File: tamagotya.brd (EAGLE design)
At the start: 27.9 x 31.8 mm, 64 parts, among them U100 ESP32-D2WD, U1000 TP4056, U1500 FS312F-G, U1550 FS8205, U200 UT-0206-P05FOLDED, U2000 MT3608, U2100 M3406, U300 4MB Flash, Y100 40Mhz 3.2X2.5

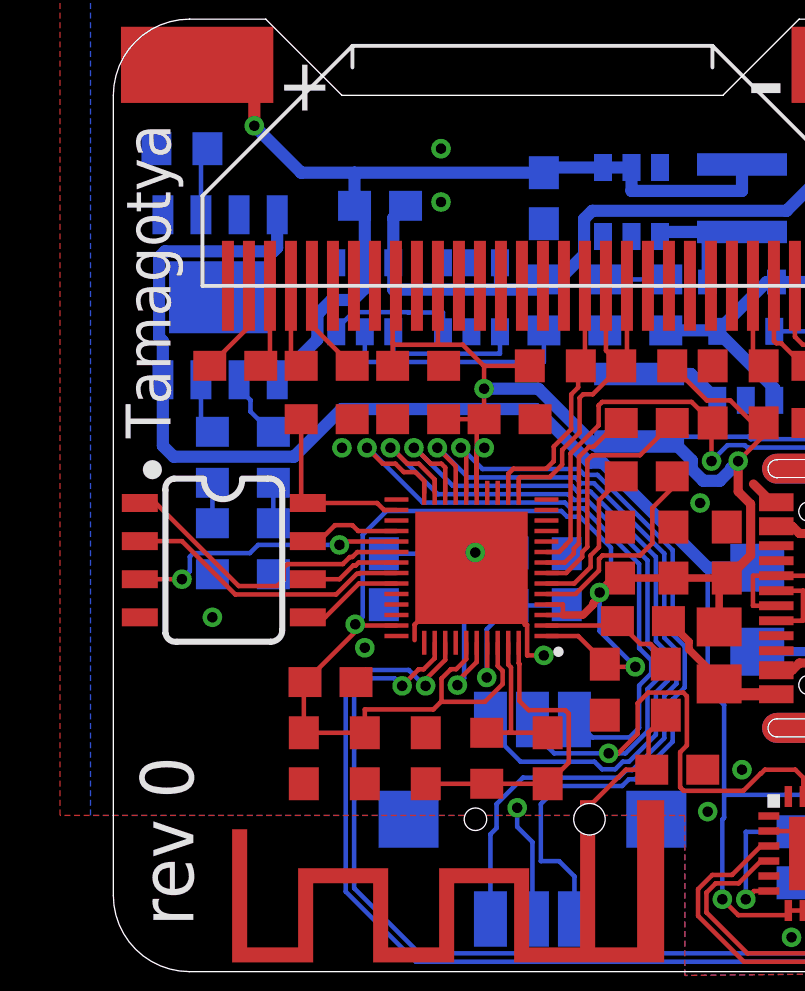
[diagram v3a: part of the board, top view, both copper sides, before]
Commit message: Accellerometer ADXL345 with i2c + 1 interrupt.
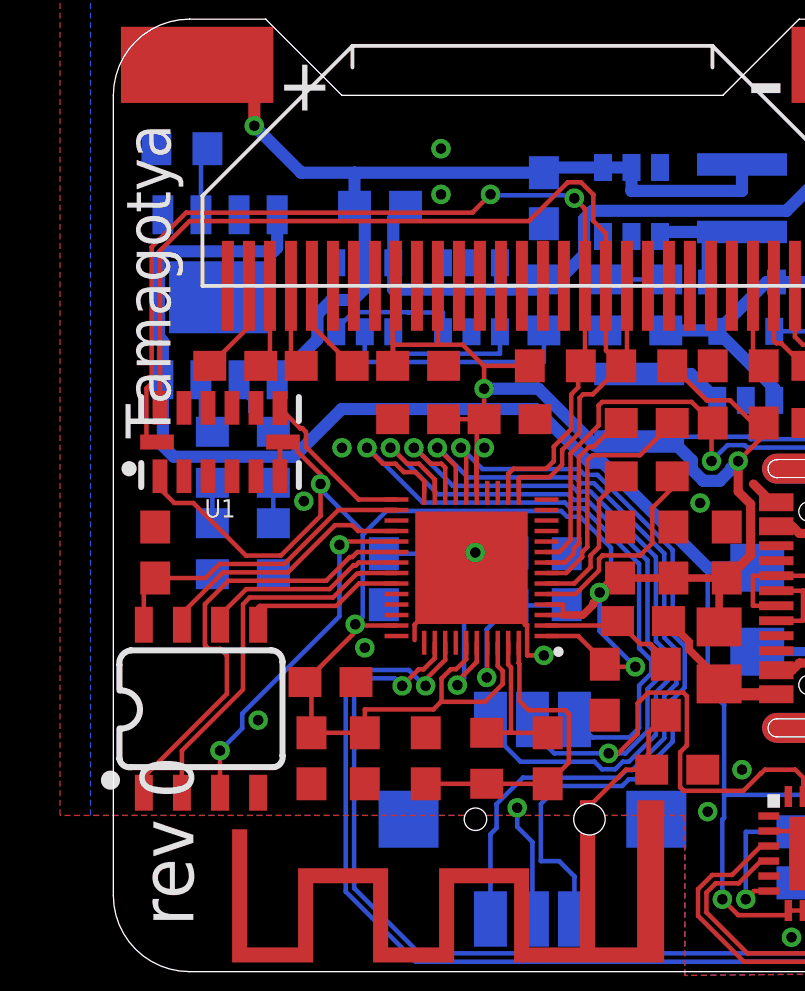
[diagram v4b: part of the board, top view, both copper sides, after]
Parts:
- added U1: ADXL345, SparkFun-Sensors:LGA-14
- moved C300 7.24 mm to (1.40, 14.0), turned to 90 degrees
- moved U300 5.01 mm to (2.92, 8.76), turned to 0 degrees
- moved C111 0.25 mm to (6.60, 7.11)
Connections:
- net 3.3V: now also U1.1, U1.6, U1.7
- net GND: now also U1.12, U1.2, U1.4, U1.5
- net GPIO16: now also U1.8
- net SCL: now also U1.14
- net SDA: now also U1.13
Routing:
- net SCL: track 8.60 -> 33.5 mm, vias 0 -> 2
- net SDA: track 12.1 -> 36.2 mm
- net 3.3V: track 91.9 -> 105.7 mm, vias 6 -> 7
- net SHD/SD2: track 3.26 -> 8.83 mm
- net VDD_SDIO: track 5.94 -> 11.4 mm
- net GPIO16: track 0.00 -> 5.43 mm
- net SCS/CMD: track 10.4 -> 15.1 mm
- net SCK/CLK: track 3.19 -> 6.92 mm
- net SDO/SD0: track 9.59 -> 12.7 mm
- net SWP/SD3: track 9.36 -> 11.9 mm
- net SDI/SD1: track 3.42 -> 5.52 mm
- net GND: vias 14 -> 15
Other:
- board text added: "TODO: Attach charge status circuitry to something ADC sensing battery voltage. DAC output for small speaker ESP32 TX/RX/RST/GPIO-0 breakout I2C breakout?"
- board text removed: "TODO: ADC sensing battery voltage. DAC output for small speaker ESP32 TX/RX/RST/GPIO-0 breakout Accellerometer would be reet grand I2C breakout?"

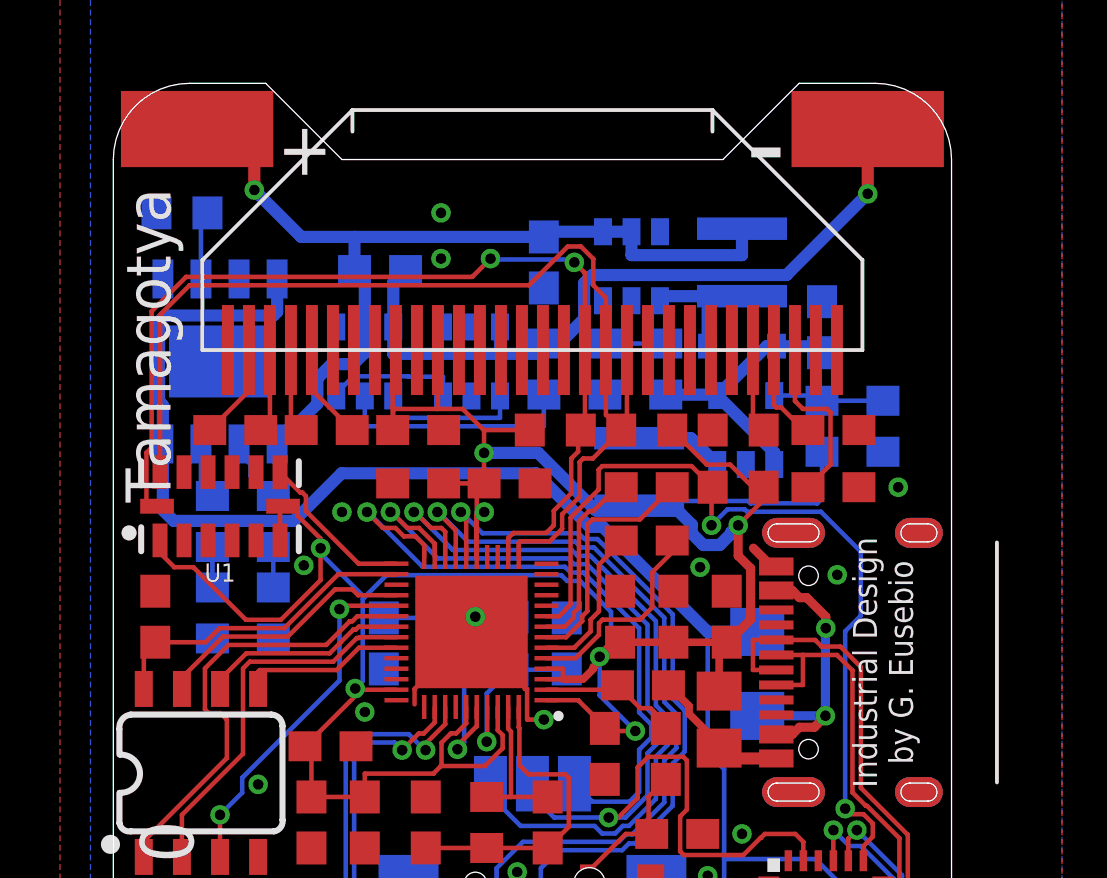
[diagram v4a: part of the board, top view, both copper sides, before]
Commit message: Done: ADC sensing battery voltage.
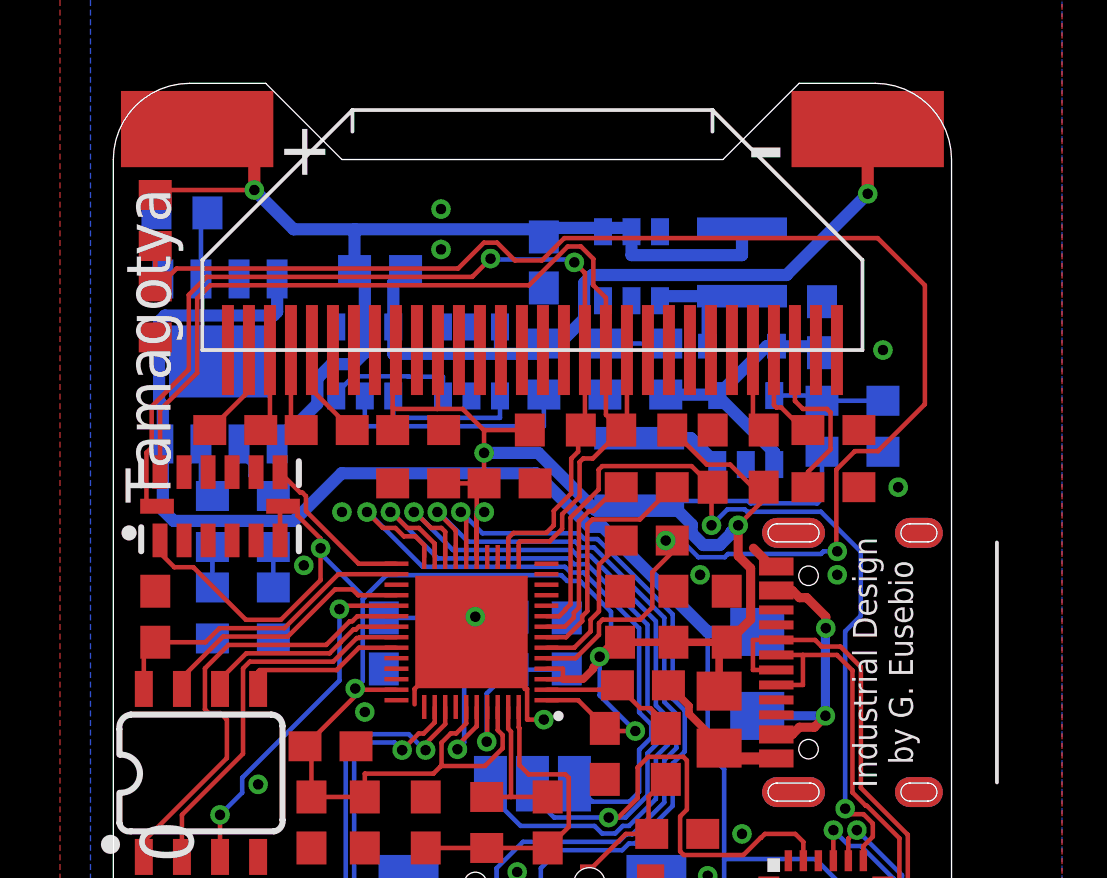
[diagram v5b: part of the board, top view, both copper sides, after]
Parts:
- added R4, R5: 20k, rcl:R0603
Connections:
- net GND: now also R5.1
- net SENSOR_VP: now also R4.1, R5.2
- net V_BATT: now also R4.2
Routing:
- net SENSOR_VP: track 6.96 -> 52.6 mm, vias 0 -> 2
- net V_BATT: track 31.6 -> 35.5 mm
- net VDD_SDIO: track 11.4 -> 10.7 mm
- net GND: vias 15 -> 16
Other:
- board text added: "TODO: DAC output for small speaker ESP32 TX/RX/RST/GPIO-0 breakout I2C breakout?"
- board text removed: "TODO: Attach charge status circuitry to something ADC sensing battery voltage. DAC output for small speaker ESP32 TX/RX/RST/GPIO-0 breakout I2C breakout?"

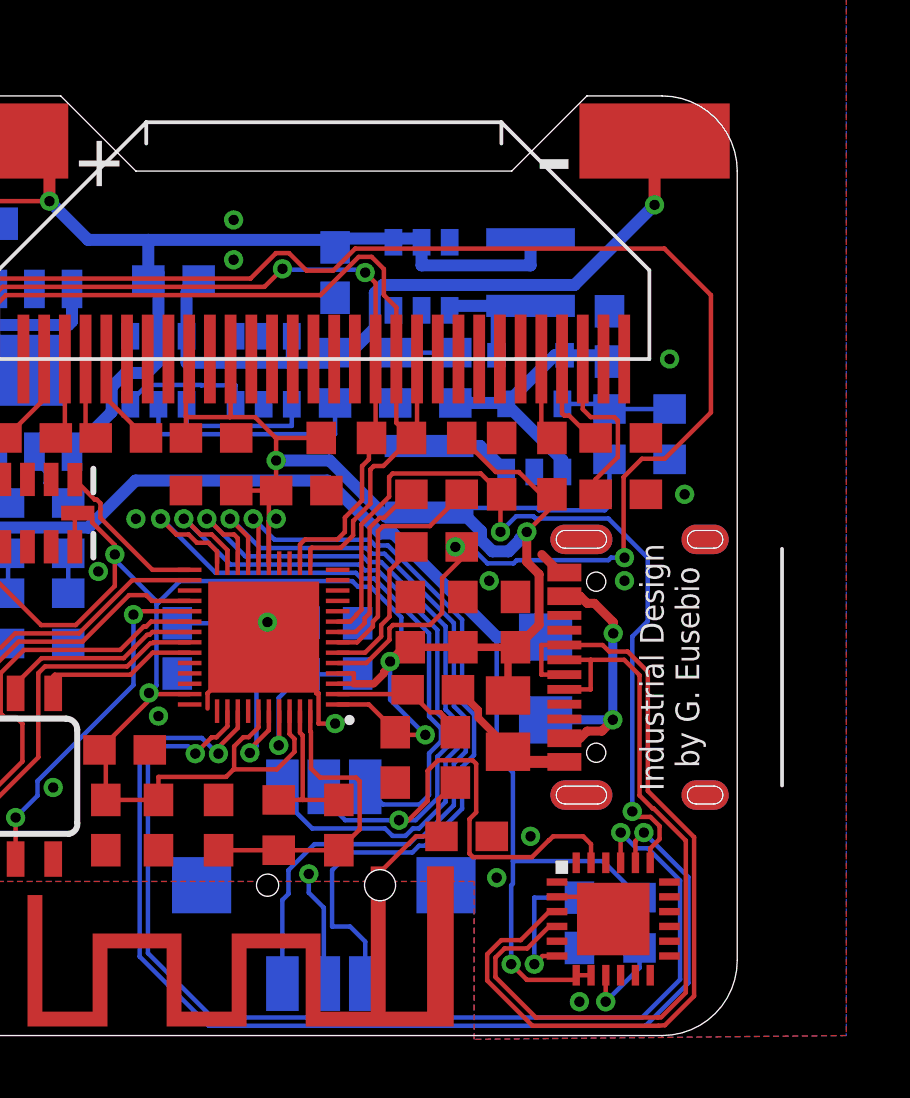
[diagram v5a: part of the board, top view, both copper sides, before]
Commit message: Add a NPN transitor to drive a piezo speaker
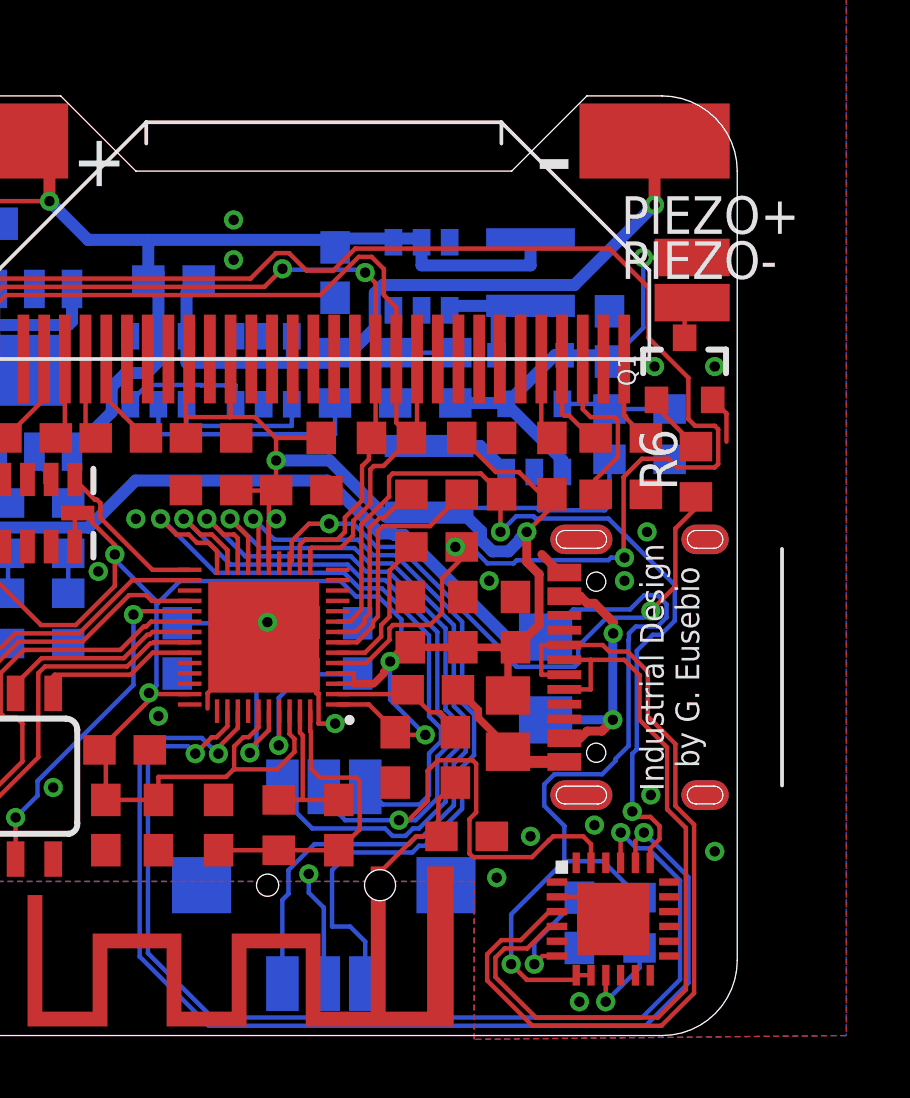
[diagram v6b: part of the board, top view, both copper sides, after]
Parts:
- added PIEZO+, PIEZO-: WIREPADSMD1,27-254, wirepad:SMD1,27-2,54
- added Q1: 600mA/40V, SparkFun-DiscreteSemi:SOT23-3
- added R6: 1k, rcl:R0603
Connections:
- new net N$5: Q1.1, R6.2
- new net PIEZO_GND: PIEZO-.1, Q1.3
- net 5V: now also PIEZO+.1
- net GND: now also Q1.2
- net GPIO14: now also R6.1
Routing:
- net GPIO14: track 0.00 -> 20.8 mm, vias 0 -> 2
- net V_USB: track 53.5 -> 61.5 mm
- net 5V: track 9.08 -> 14.7 mm, vias 0 -> 1
- net GND: track 21.5 -> 26.1 mm, vias 16 -> 20
- net N$5: track 0.00 -> 2.13 mm
- net PIEZO_GND: track 0.00 -> 1.29 mm
- net RESET: track 28.3 -> 29.3 mm
- net SENSOR_VP: track 52.6 -> 53.5 mm
- net CP3V3: track 4.65 -> 3.76 mm
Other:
- board text added: "TODO: ESP32 TX/RX/RST/GPIO-0 breakout I2C breakout?"
- board text removed: "TODO: DAC output for small speaker ESP32 TX/RX/RST/GPIO-0 breakout I2C breakout?"
